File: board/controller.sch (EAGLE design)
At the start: 69 parts, among them J1 COOLANT, J10 FEED_HOLD, J11 SD_READER, J12 RESET, J13 Z, J14 GND, J15 Z_DISPLAY, J18 DISPLAY, J19 A, J2 PROBE, J20 HOLDING, J22 WHEEL, J23 SPINDLE, J24 +5V, J26 GND, J3 MOTOR_CURRENT, J4 X, J6 ERROR, J8 CYCLE_START, J9 Y, U100 SENSOR-IR-THRU

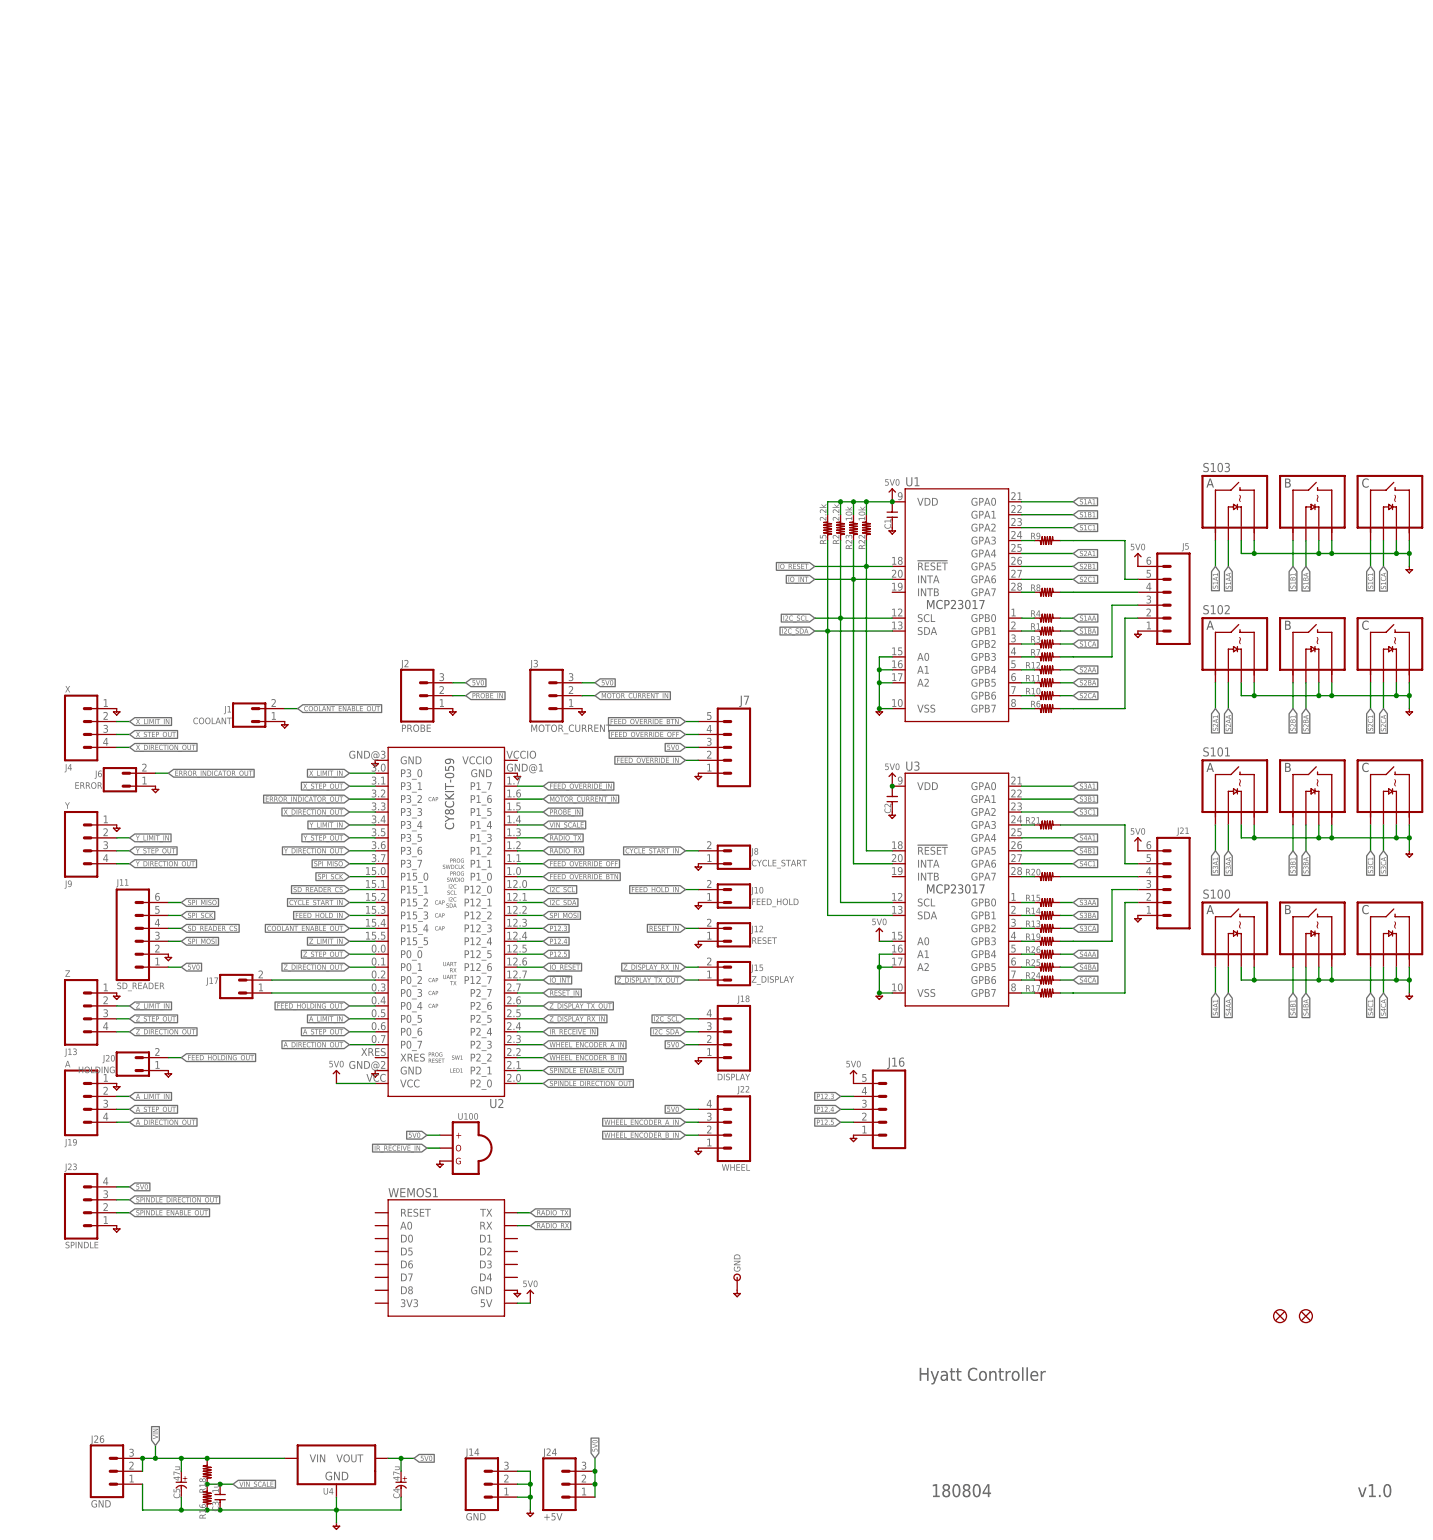
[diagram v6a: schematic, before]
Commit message: re-organizing pin layout due to creator optimization
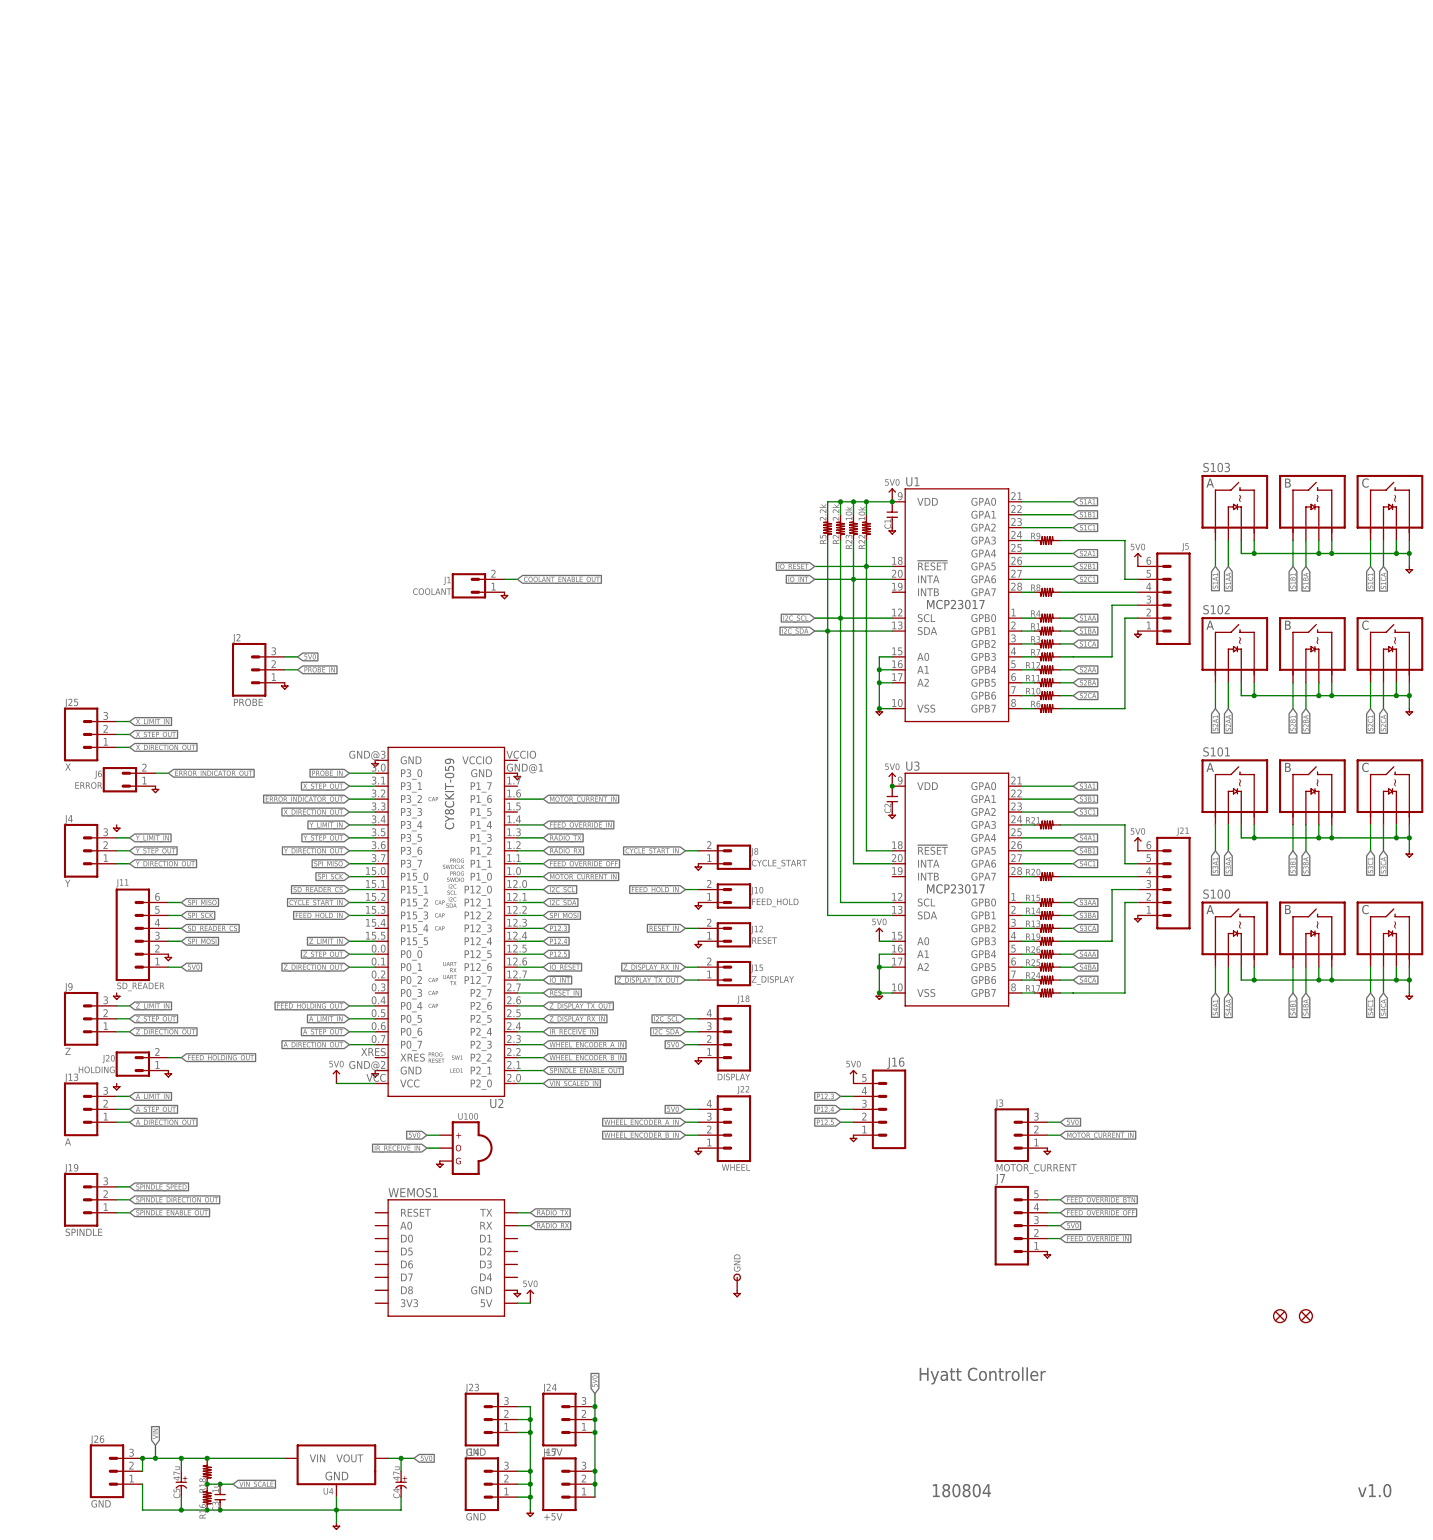
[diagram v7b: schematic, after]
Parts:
- added J25: X, holla:CONN-03-3.81MM-PLUGIN-SCREW
- J13: value Z -> A; device holla:CONN-04-3.81MM-PLUGIN-SCREW -> holla:CONN-03-3.81MM-PLUGIN-SCREW
- J17: value (none) -> +5V; device holla:CONN-02-0.1 -> holla:CONN-03-3.81MM-PLUGIN-SCREW
- J19: value A -> SPINDLE; device holla:CONN-04-3.81MM-PLUGIN-SCREW -> holla:CONN-03-3.81MM-PLUGIN-SCREW
- J23: value SPINDLE -> GND; device holla:CONN-04-3.81MM-PLUGIN-SCREW -> holla:CONN-03-3.81MM-PLUGIN-SCREW
- J4: value X -> Y; device holla:CONN-04-3.81MM-PLUGIN-SCREW -> holla:CONN-03-3.81MM-PLUGIN-SCREW
- J9: value Y -> Z; device holla:CONN-04-3.81MM-PLUGIN-SCREW -> holla:CONN-03-3.81MM-PLUGIN-SCREW
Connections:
- removed net N$43: J17.2, U2.P0_2
- removed net N$45: J17.1, U2.P0_3
- new net SPINDLE_SPEED: J19.3
- new net VIN_SCALED_IN: U2.P2_0
- net 5V0: now also J17.1, J17.2, J17.3; no longer J23.4
- net A_DIRECTION_OUT: now also J13.1; no longer J19.4
- net A_LIMIT_IN: now also J13.3; no longer J19.2
- net A_STEP_OUT: now also J13.2; no longer J19.3
- net COOLANT_ENABLE_OUT: no longer U2.P15_4
- net FEED_OVERRIDE_BTN: no longer U2.P1_0
- net FEED_OVERRIDE_IN: now also U2.P1_4; no longer U2.P1_7
- net GND: now also J23.2, J23.3; no longer J13.1, J19.1, J4.1, J9.1
- net MOTOR_CURRENT_IN: now also U2.P1_0
- net PROBE_IN: now also U2.P3_0; no longer U2.P1_5
- net SPINDLE_DIRECTION_OUT: now also J19.2; no longer J23.3, U2.P2_0
- net SPINDLE_ENABLE_OUT: now also J19.1; no longer J23.2
- net VIN_SCALE: no longer U2.P1_4
- net X_DIRECTION_OUT: now also J25.1; no longer J4.4
- net X_LIMIT_IN: now also J25.3; no longer J4.2, U2.P3_0
- net X_STEP_OUT: now also J25.2; no longer J4.3
- net Y_DIRECTION_OUT: now also J4.1; no longer J9.4
- net Y_LIMIT_IN: now also J4.3; no longer J9.2
- net Y_STEP_OUT: now also J4.2; no longer J9.3
- net Z_DIRECTION_OUT: now also J9.1; no longer J13.4
- net Z_LIMIT_IN: now also J9.3; no longer J13.2
- net Z_STEP_OUT: now also J9.2; no longer J13.3
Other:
- moved on the sheet: J1, J2, J24, J3, J7

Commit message: reworked connector positions and pin mapping
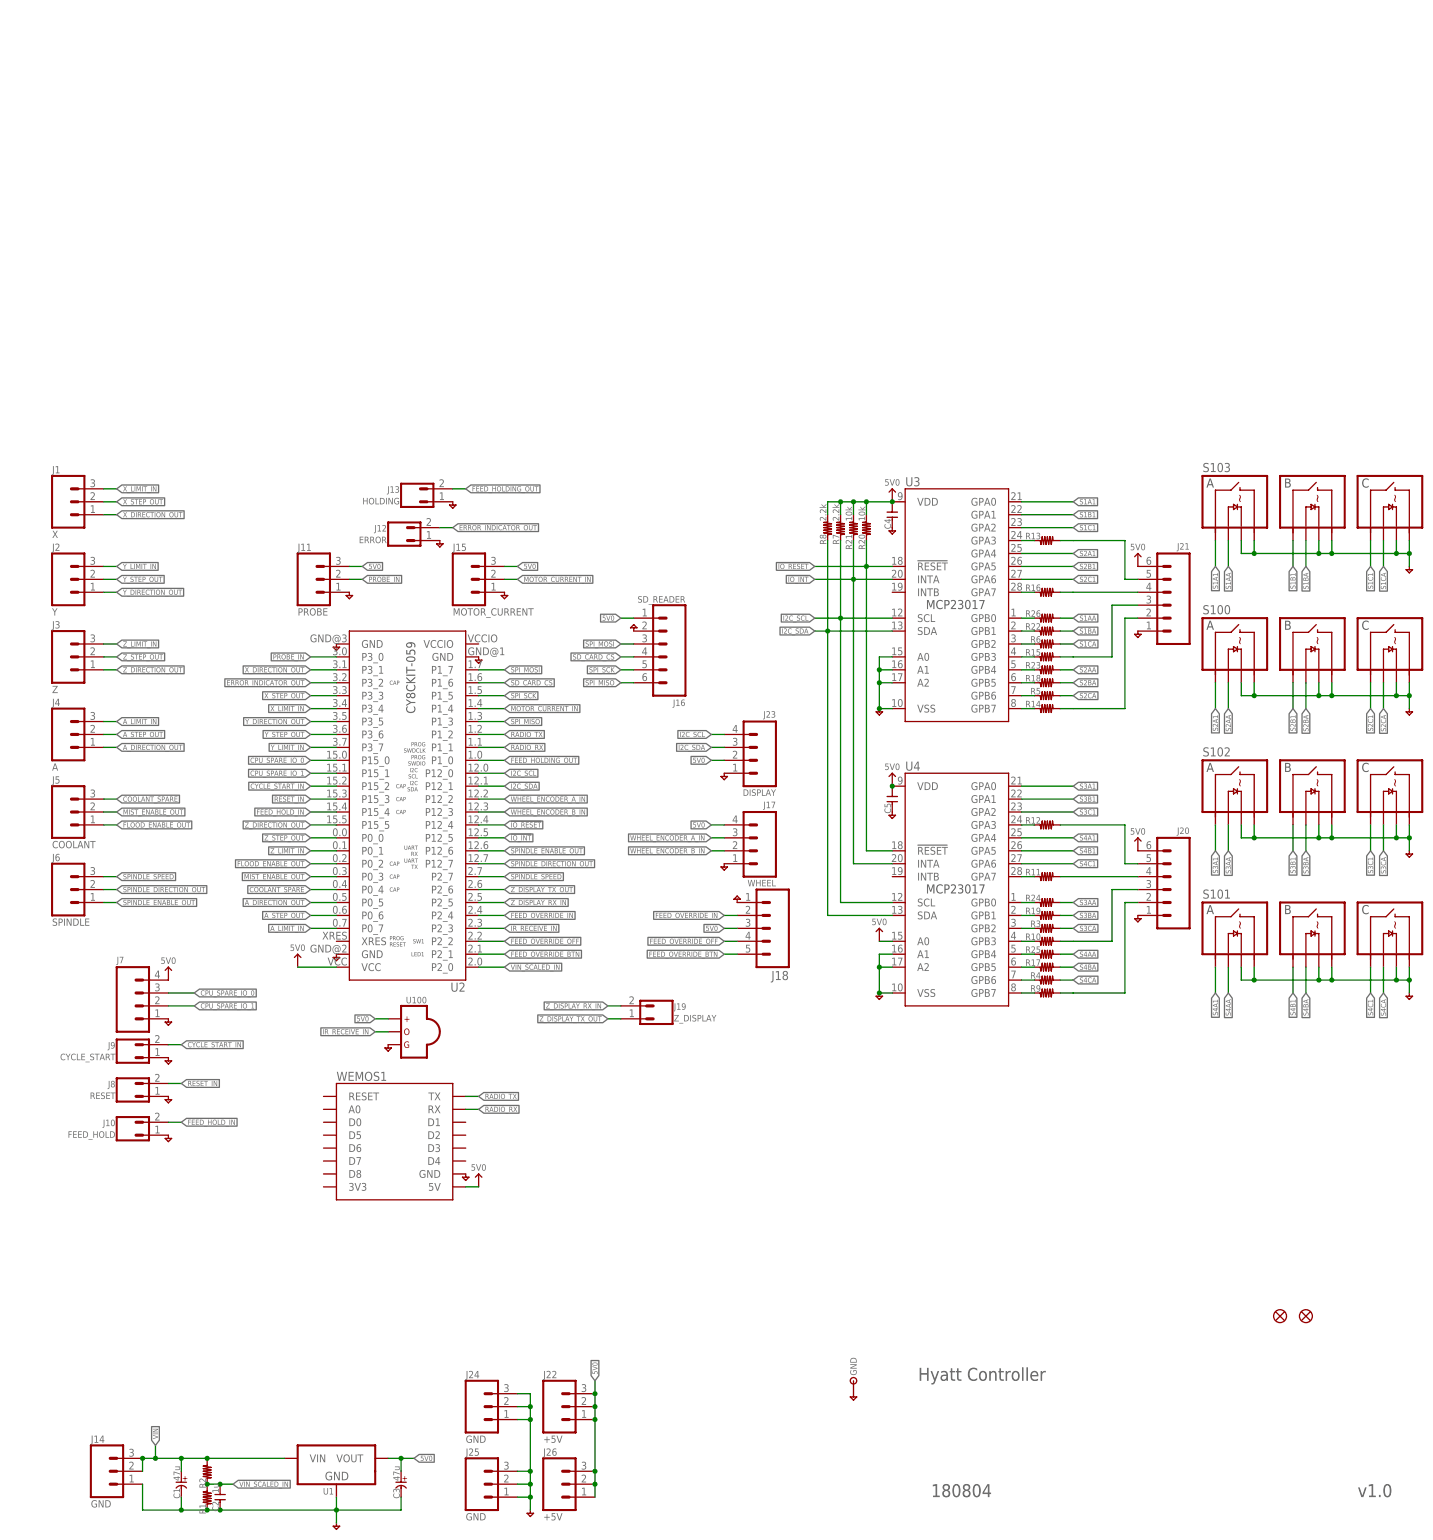
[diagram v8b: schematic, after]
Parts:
- C1: value (none) -> 47u; device holla:C-0603 -> holla:C-POLARIZED-E5-10
- C2: value (none) -> 1u
- C3: value 1u -> 47u; device holla:C-0603 -> holla:C-POLARIZED-E5-10
- C4, C5: value 47u -> (none); device holla:C-POLARIZED-E5-10 -> holla:C-0603
- J1: value COOLANT -> X; device holla:CONN-02-3.81MM-PLUGIN-SCREW -> holla:CONN-03-3.81MM-PLUGIN-SCREW
- J11: value SD_READER -> PROBE; device holla:CONN-06-0.1 -> holla:CONN-03-3.81MM-PLUGIN-SCREW
- J12: value RESET -> ERROR
- J13: value A -> HOLDING; device holla:CONN-03-3.81MM-PLUGIN-SCREW -> holla:CONN-02-.100-VERT-HEADER
- J15: value Z_DISPLAY -> MOTOR_CURRENT; device holla:CONN-02-3.81MM-PLUGIN-SCREW -> holla:CONN-03-3.81MM-PLUGIN-SCREW
- J16: value (none) -> SD_READER; device holla:CONN-05-.100-VERT-HEADER -> holla:CONN-06-0.1
- J17: value +5V -> WHEEL; device holla:CONN-03-3.81MM-PLUGIN-SCREW -> holla:CONN-04-.100-VERT-HEADER
- J18: value DISPLAY -> (none); device holla:CONN-04-.100-VERT-HEADER -> holla:CONN-05-PTH
- J19: value SPINDLE -> Z_DISPLAY; device holla:CONN-03-3.81MM-PLUGIN-SCREW -> holla:CONN-02-3.81MM-PLUGIN-SCREW
- J2: value PROBE -> Y
- J20: value HOLDING -> (none); device holla:CONN-02-.100-VERT-HEADER -> holla:CONN-06-.100-VERT-HEADER
- J22: value WHEEL -> +5V; device holla:CONN-04-.100-VERT-HEADER -> holla:CONN-03-3.81MM-PLUGIN-SCREW
- J23: value GND -> DISPLAY; device holla:CONN-03-3.81MM-PLUGIN-SCREW -> holla:CONN-04-.100-VERT-HEADER
- J24: value +5V -> GND
- J25: value X -> GND
- J26: value GND -> +5V
- J3: value MOTOR_CURRENT -> Z
- J4: value Y -> A
- J5: value (none) -> COOLANT; device holla:CONN-06-.100-VERT-HEADER -> holla:CONN-03-3.81MM-PLUGIN-SCREW
- J6: value ERROR -> SPINDLE; device holla:CONN-02-.100-VERT-HEADER -> holla:CONN-03-3.81MM-PLUGIN-SCREW
- J7: device holla:CONN-05-PTH -> holla:CONN-04-0.1
- J8: value CYCLE_START -> RESET
- J9: value Z -> CYCLE_START; device holla:CONN-03-3.81MM-PLUGIN-SCREW -> holla:CONN-02-.100-VERT-HEADER
- R2, R5: value 2.2k -> (none)
- R20, R21: value (none) -> 10k
- R22, R23: value 10k -> (none)
- R7, R8: value (none) -> 2.2k
- U1: device holla:IO-MCP23017SO -> holla:VREG-SIP3
- U4: device holla:VREG-SIP3 -> holla:IO-MCP23017SO
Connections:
- removed net COOLANT_ENABLE_OUT: J1.2
- removed net P12.3: J16.4, U2.P12_3
- removed net P12.4: J16.3, U2.P12_4
- removed net P12.5: J16.2, U2.P12_5
- removed net SD_READER_CS: J11.4, U2.P15_1
- removed net VIN_SCALE: C3.1, R16.2, R18.1
- new net COOLANT_SPARE: J5.3, U2.P0_4
- new net CPU_SPARE_IO_0: J7.3, U2.P15_0
- new net CPU_SPARE_IO_1: J7.2, U2.P15_1
- new net FLOOD_ENABLE_OUT: J5.1, U2.P0_2
- new net MIST_ENABLE_OUT: J5.2, U2.P0_3
- new net SD_CARD_CS: J16.4, U2.P1_6
- net !IO_INT: now also R21.1, U2.P12_5, U4.INTA; no longer R23.1, U1.INTA, U2.P12_7
- net !IO_RESET: now also R20.1, U2.P12_4, U4.!RESET; no longer R22.1, U1.!RESET, U2.P12_6
- net 5V0: now also C3.+, C4.1, C5.1, J11.3, J15.3, J16.1, J17.4, J18.3, J20.6, J22.1, J22.2, J22.3, J23.2, J26.1, J26.2, J26.3, J7.4, R20.2, R21.2, R7.2, R8.2, U1.VOUT, U4.A0, U4.VDD; no longer C1.1, C2.1, C4.+, J11.1, J16.5, J17.1, J17.2, J17.3, J18.2, J2.3, J22.4, J24.1, J24.2, J24.3, J3.3, J5.6, J7.3, R2.2, R22.2, R23.2, R5.2, U1.VDD, U3.A0, U4.VOUT
- net A_DIRECTION_OUT: now also J4.1, U2.P0_5; no longer J13.1, U2.P0_7
- net A_LIMIT_IN: now also J4.3, U2.P0_7; no longer J13.3, U2.P0_5
- net A_STEP_OUT: now also J4.2; no longer J13.2
- net CYCLE_START_IN: now also J9.2; no longer J8.2
- net ERROR_INDICATOR_OUT: now also J12.2; no longer J6.2
- net FEED_HOLDING_OUT: now also J13.2, U2.P1_0; no longer J20.2, U2.P0_4
- net FEED_HOLD_IN: now also U2.P15_4; no longer U2.P15_3
- net FEED_OVERRIDE_BTN: now also J18.5, U2.P2_1; no longer J7.5
- net FEED_OVERRIDE_IN: now also J18.2, U2.P2_4; no longer J7.2, U2.P1_4
- net FEED_OVERRIDE_OFF: now also J18.4, U2.P2_2; no longer J7.4, U2.P1_1
- net GND: now also C1.-, C3.-, C4.2, C5.2, J11.1, J13.1, J15.1, J16.2, J17.1, J24.1, J24.2, J24.3, J25.1, J25.2, J25.3, J9.1, R1.1, U1.GND, U3.A0, U4.A1, U4.A2, U4.VSS; no longer C1.2, C3.2, C4.-, C5.-, J1.1, J11.2, J14.2, J14.3, J16.1, J2.1, J22.1, J23.2, J23.3, J26.1, J3.1, J5.1, J6.1, R16.1, U1.A0, U1.A1, U1.A2, U1.VSS, U4.GND
- net I2C_SCL: now also J23.4, R7.1, U4.SCL; no longer J18.4, R2.1, U1.SCL
- net I2C_SDA: now also J23.3, R8.1, U4.SDA; no longer J18.3, R5.1, U1.SDA
- net IR_RECEIVE_IN: now also U2.P2_3; no longer U2.P2_4
- net MOTOR_CURRENT_IN: now also J15.2, U2.P1_4; no longer J3.2, U2.P1_0, U2.P1_6
- net N$1: now also R26.1, U3.GPB0; no longer R4.1, U1.GPB0
- net N$10: now also J20.5, R12.2; no longer J21.5, R21.2
- net N$11: now also J20.4, R11.2; no longer J21.4, R20.2
- net N$15: now also R6.1, U3.GPB2; no longer R3.1, U1.GPB2
- net N$16: now also R15.1, U3.GPB3; no longer R7.1, U1.GPB3
- net N$17: now also R23.1, U3.GPB4; no longer R12.1, U1.GPB4
- net N$18: now also R18.1, U3.GPB5; no longer R11.1, U1.GPB5
- net N$19: now also R5.1, U3.GPB6; no longer R10.1, U1.GPB6
- net N$2: now also R22.1, U3.GPB1; no longer R1.1, U1.GPB1
- net N$20: now also R14.1, U3.GPB7; no longer R6.1, U1.GPB7
- net N$21: now also R24.1, U4.GPB0; no longer R15.1, U3.GPB0
- net N$22: now also R19.1, U4.GPB1; no longer R14.1, U3.GPB1
- net N$23: now also R3.1, U4.GPB2; no longer R13.1, U3.GPB2
- net N$24: now also R10.1, U4.GPB3; no longer R19.1, U3.GPB3
- net N$25: now also R25.1, U4.GPB4; no longer R26.1, U3.GPB4
- net N$26: now also R17.1, U4.GPB5; no longer R25.1, U3.GPB5
- net N$27: now also R4.1, U4.GPB6; no longer R24.1, U3.GPB6
- net N$28: now also R9.1, U4.GPB7; no longer R17.1, U3.GPB7
- net N$3: now also R13.1, U3.GPA3; no longer R9.1, U1.GPA3
- net N$30: now also J21.2, R14.2; no longer J5.2, R6.2
- net N$4: now also J21.5, R13.2; no longer J5.5, R9.2
- net N$44: now also J20.3, R10.2; no longer J21.3, R19.2
- net N$48: now also J20.2, R9.2; no longer J21.2, R17.2
- net N$5: now also R16.1, U3.GPA7; no longer R8.1, U1.GPA7
- net N$6: now also J21.3, R15.2; no longer J5.3, R7.2
- net N$7: now also J21.4, R16.2; no longer J5.4, R8.2
- net N$8: now also R12.1, U4.GPA3; no longer R21.1, U3.GPA3
- net N$9: now also R11.1, U4.GPA7; no longer R20.1, U3.GPA7
- net PROBE_IN: now also J11.2; no longer J2.2
- net RADIO_RX: now also U2.P1_1; no longer U2.P1_2
- net RADIO_TX: now also U2.P1_2; no longer U2.P1_3
- net RESET_IN: now also J8.2, U2.P15_3; no longer J12.2, U2.P2_7
- net S1A1: now also U3.GPA0; no longer U1.GPA0
- net S1AA: now also R26.2; no longer R4.2
- net S1B1: now also U3.GPA1; no longer U1.GPA1
- net S1BA: now also R22.2; no longer R1.2
- net S1C1: now also U3.GPA2; no longer U1.GPA2
- net S1CA: now also R6.2; no longer R3.2
- net S2A1: now also S100.A_1, U3.GPA4; no longer S102.A_1, U1.GPA4
- net S2AA: now also R23.2, S100.A_A; no longer R12.2, S102.A_A
- net S2B1: now also S100.B_1, U3.GPA5; no longer S102.B_1, U1.GPA5
- net S2BA: now also R18.2, S100.B_A; no longer R11.2, S102.B_A
- net S2C1: now also S100.C_1, U3.GPA6; no longer S102.C_1, U1.GPA6
- net S2CA: now also R5.2, S100.C_A; no longer R10.2, S102.C_A
- net S3A1: now also S102.A_1, U4.GPA0; no longer S101.A_1, U3.GPA0
- net S3AA: now also R24.2, S102.A_A; no longer R15.2, S101.A_A
- net S3B1: now also S102.B_1, U4.GPA1; no longer S101.B_1, U3.GPA1
- net S3BA: now also R19.2, S102.B_A; no longer R14.2, S101.B_A
- net S3C1: now also S102.C_1, U4.GPA2; no longer S101.C_1, U3.GPA2
- net S3CA: now also R3.2, S102.C_A; no longer R13.2, S101.C_A
- net S4A1: now also S101.A_1, U4.GPA4; no longer S100.A_1, U3.GPA4
- net S4AA: now also R25.2, S101.A_A; no longer R26.2, S100.A_A
- net S4B1: now also S101.B_1, U4.GPA5; no longer S100.B_1, U3.GPA5
- net S4BA: now also R17.2, S101.B_A; no longer R25.2, S100.B_A
- net S4C1: now also S101.C_1, U4.GPA6; no longer S100.C_1, U3.GPA6
- net S4CA: now also R4.2, S101.C_A; no longer R24.2, S100.C_A
- net SPINDLE_DIRECTION_OUT: now also J6.2, U2.P12_7; no longer J19.2
- net SPINDLE_ENABLE_OUT: now also J6.1, U2.P12_6; no longer J19.1, U2.P2_1
- net SPINDLE_SPEED: now also J6.3, U2.P2_7; no longer J19.3
- net SPI_MISO: now also J16.6, U2.P1_3; no longer J11.6, U2.P3_7
- net SPI_MOSI: now also J16.3, U2.P1_7; no longer J11.3, U2.P12_2
- net SPI_SCK: now also J16.5, U2.P1_5; no longer J11.5, U2.P15_0
- net VIN: now also C1.+, J14.2, J14.3, R2.2, U1.VIN; no longer C5.+, J26.2, J26.3, R18.2, U4.VIN
- net VIN_SCALED_IN: now also C2.1, R1.2, R2.1
- net WHEEL_ENCODER_A_IN: now also J17.3, U2.P12_2; no longer J22.3, U2.P2_3
- net WHEEL_ENCODER_B_IN: now also J17.2, U2.P12_3; no longer J22.2, U2.P2_2
- net X_DIRECTION_OUT: now also J1.1, U2.P3_1; no longer J25.1, U2.P3_3
- net X_LIMIT_IN: now also J1.3, U2.P3_4; no longer J25.3
- net X_STEP_OUT: now also J1.2, U2.P3_3; no longer J25.2, U2.P3_1
- net Y_DIRECTION_OUT: now also J2.1, U2.P3_5; no longer J4.1, U2.P3_6
- net Y_LIMIT_IN: now also J2.3, U2.P3_7; no longer J4.3, U2.P3_4
- net Y_STEP_OUT: now also J2.2, U2.P3_6; no longer J4.2, U2.P3_5
- net Z_DIRECTION_OUT: now also J3.1, U2.P15_5; no longer J9.1, U2.P0_1
- net Z_DISPLAY_RX_IN: now also J19.2; no longer J15.2
- net Z_DISPLAY_TX_OUT: now also J19.1; no longer J15.1
- net Z_LIMIT_IN: now also J3.3, U2.P0_1; no longer J9.3, U2.P15_5
- net Z_STEP_OUT: now also J3.2; no longer J9.2
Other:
- moved on the sheet: C2, GND, J10, J12, J14, J2, J21, J24, J25, J26, J3, J4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
